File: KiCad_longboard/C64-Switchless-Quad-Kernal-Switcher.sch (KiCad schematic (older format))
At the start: 9 parts, among them J1 Pinlist_12pin, J2 Pinlist_12pin, J3 27C256_28PDIP, J4 Wireconnections, U1 ATtiny85-20PU

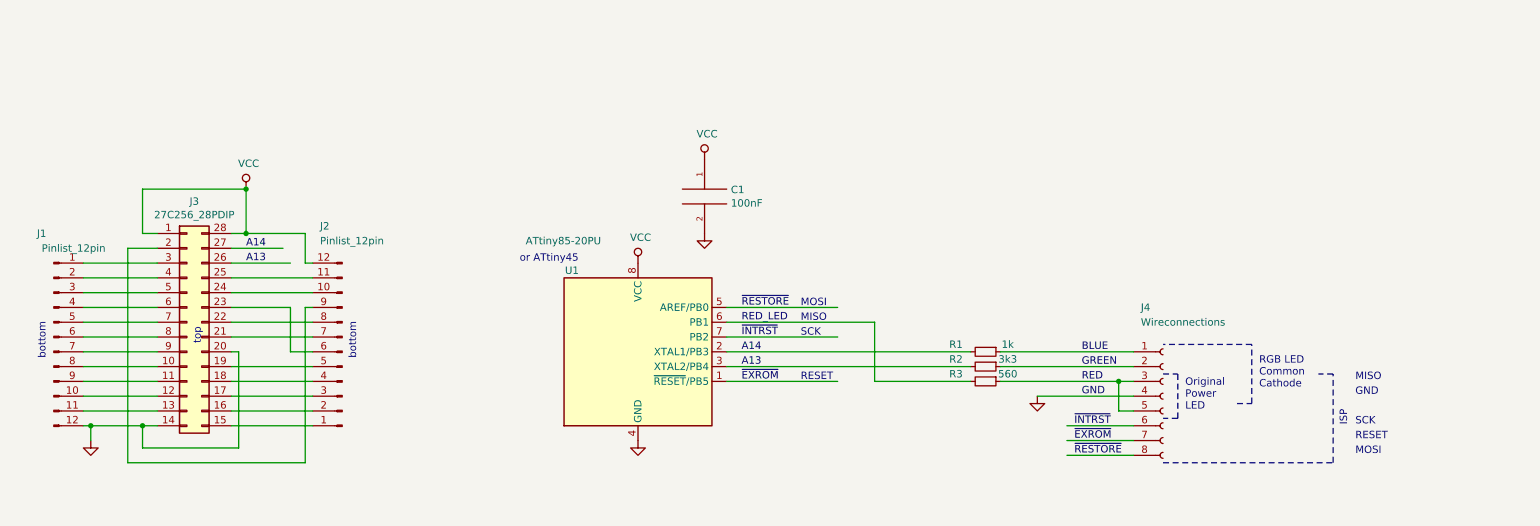
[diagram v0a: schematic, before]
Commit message: longboard pcb version, 8 bank support
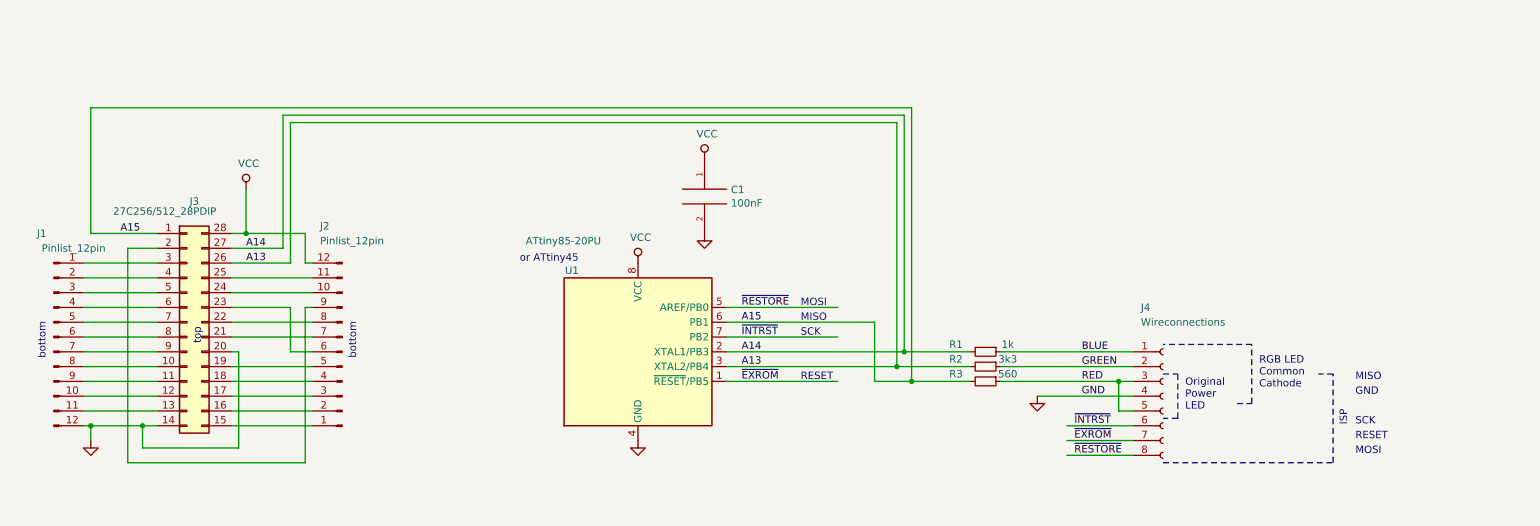
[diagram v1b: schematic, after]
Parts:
- J3: value 27C256_28PDIP -> 27C256/512_28PDIP
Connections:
- net labels added: A15
- net labels removed: RED_LED
- wire segments 64 -> 74
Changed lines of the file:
@@
 Sheet 1 1
 Title "C64 Switchless Quad Kernal Switcher (SKS64)"
-Date "2019-07-15"
-Rev "1.20"
+Date "2019-07-23"
+Rev "1.21"
 Comp "Bwack"
 Comment1 ""
@@
 P 1850 4900
 F 0 "J3" H 1900 5717 50  0000 C CNN
-F 1 "27C256_28PDIP" H 1900 5626 50  0000 C CNN
+F 1 "27C256/512_28PDIP" H 1700 5650 50  0000 C CNN
 F 2 "Package_DIP:DIP-28_W15.24mm_Socket" H 1850 4900 50  0001 C CNN
 F 3 "~" H 1850 4900 50  0001 C CNN
@@
 	2650 4300 2250 4300
 Wire Wire Line
-	1650 4300 1550 4300
-Wire Wire Line
-	1550 4300 1550 4000
-Wire Wire Line
-	1550 4000 2250 4000
-Wire Wire Line
 	2250 4000 2250 4300
 Connection ~ 2250 4300
@@
 	1    0    0    -1
 $EndComp
-Connection ~ 2250 4000
 Text Label 5600 5200 0    50   ~ 0
 A13
@@
 Text Label 5600 5000 0    50   ~ 0
 ~INTRST~
-Text Label 5600 4900 0    50   ~ 0
-RED_LED
 Text Label 5600 5300 0    50   ~ 0
 ~EXROM~
@@
 MOSI
 Wire Wire Line
-	5500 5100 7150 5100
-Wire Wire Line
-	5500 5200 7150 5200
+	5500 5100 6700 5100
+Wire Wire Line
+	5500 5200 6650 5200
 Wire Wire Line
 	5500 5300 6250 5300
 Wire Wire Line
-	7150 5300 6500 5300
+	7150 5300 6750 5300
 Wire Wire Line
 	6500 5300 6500 4900
@@
 Text Notes 4100 4500 0    50   ~ 0
 or ATtiny45
+Text Label 1400 4300 0    50   ~ 0
+A15
+Text Label 5600 4900 0    50   ~ 0
+A15
+Wire Wire Line
+	2500 4400 2500 3500
+Wire Wire Line
+	2500 3500 6700 3500
+Wire Wire Line
+	6700 3500 6700 5100
+Connection ~ 6700 5100
+Wire Wire Line
+	6700 5100 7150 5100
+Wire Wire Line
+	2550 4500 2550 3550
+Wire Wire Line
+	2550 3550 6650 3550
+Wire Wire Line
+	6650 3550 6650 5200
+Connection ~ 6650 5200
+Wire Wire Line
+	6650 5200 7150 5200
+Wire Wire Line
+	1200 4300 1200 3450
+Wire Wire Line
+	1200 3450 6750 3450
+Wire Wire Line
+	6750 3450 6750 5300
+Wire Wire Line
+	1200 4300 1650 4300
+Connection ~ 6750 5300
+Wire Wire Line
+	6750 5300 6500 5300
 $EndSCHEMATC

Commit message: shortboard version schematics added to user guide
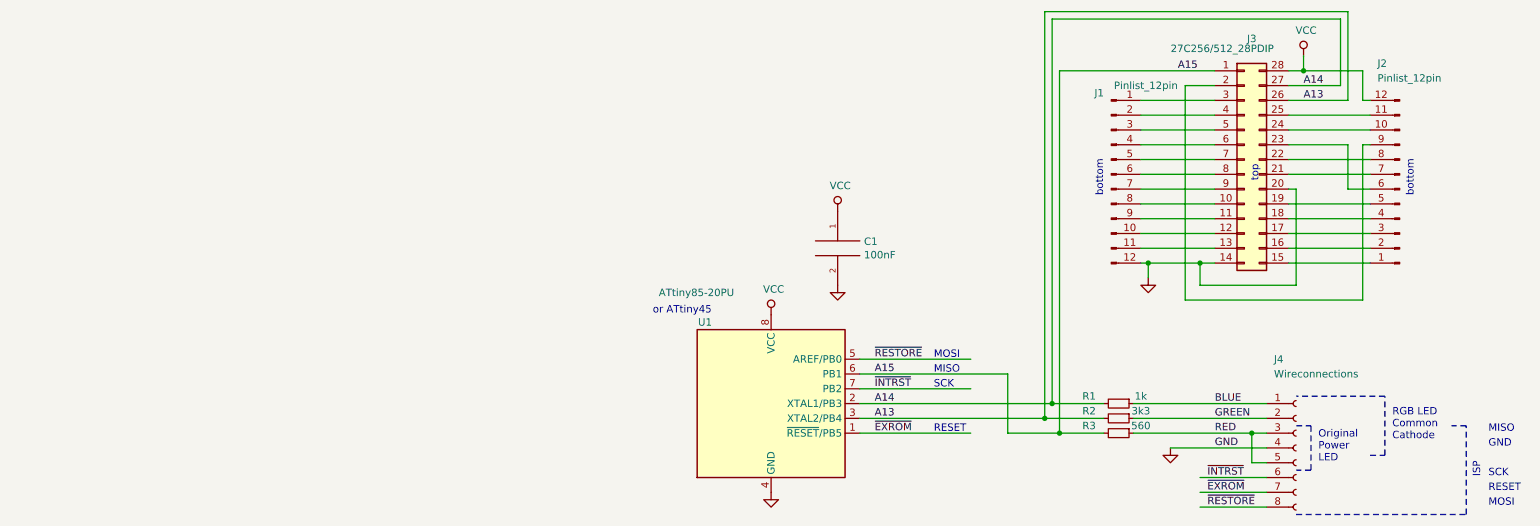
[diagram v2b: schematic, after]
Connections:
- wire segments 74 -> 72
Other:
- moved on the sheet: C1, J1, J2, J3, J4, R1, R2, R3, U1

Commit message: 1541C support in firmware and SKS64 shortboard pcb version
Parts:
- U1: symbol MCU_Microchip_ATtiny:ATtiny85-20PU -> C64-Switchless-Quad-Kernal-Switcher-rescue:ATtiny85-20PU-MCU_Microchip_ATtiny
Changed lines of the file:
@@
 EESchema Schematic File Version 4
-LIBS:C64-Switchless-Quad-Kernal-Switcher-cache
-EELAYER 29 0
+EELAYER 30 0
 EELAYER END
 $Descr A4 11693 8268
@@
 	6400 5250 7400 5250
 $Comp
-L MCU_Microchip_ATtiny:ATtiny85-20PU U1
+L C64-Switchless-Quad-Kernal-Switcher-rescue:ATtiny85-20PU-MCU_Microchip_ATtiny U1
 U 1 1 5D2A0255
 P 5800 5450
